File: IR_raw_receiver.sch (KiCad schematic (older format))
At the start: 22 parts, among them IC1 ATtiny85, P1 CONN_6, Q1 8MHz, U1 TSOP38238, U2 L78L05

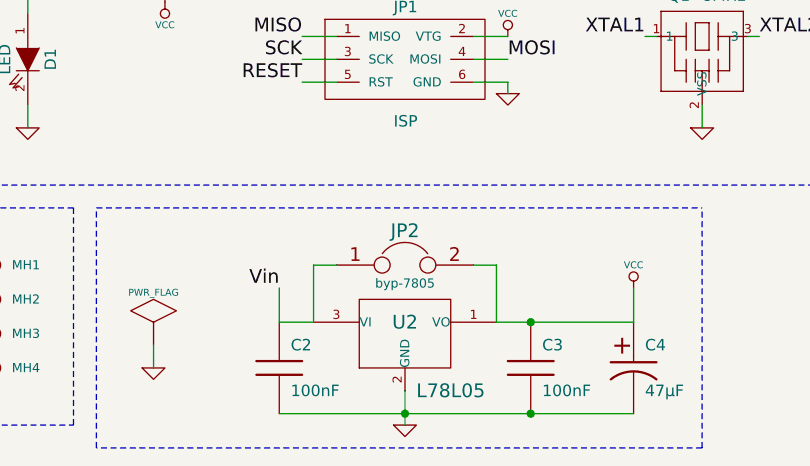
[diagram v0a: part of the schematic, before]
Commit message: V1.20 = shrinked version of V1.10 (standing resistors...)
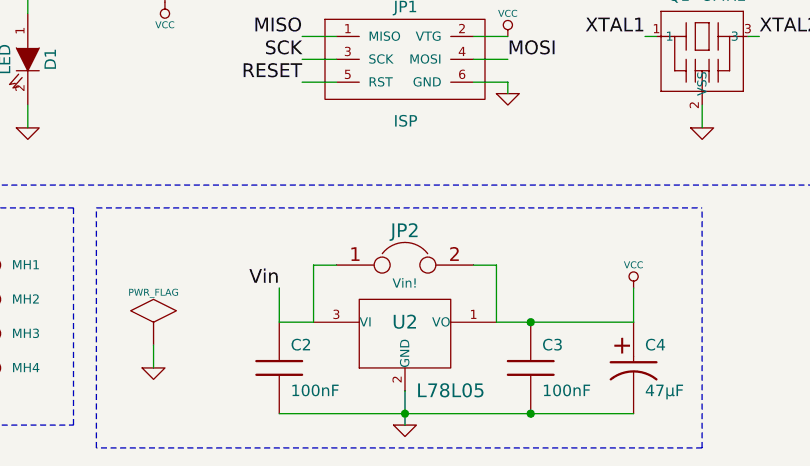
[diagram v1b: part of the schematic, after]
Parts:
- JP2: value byp-7805 -> Vin!
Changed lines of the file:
@@
-EESchema Schematic File Version 2  date Sat 31 Mar 2012 04:20:52 PM CEST
+EESchema Schematic File Version 2  date Sat 31 Mar 2012 08:07:43 PM CEST
 LIBS:power
 LIBS:device
@@
 Title "IR_raw_receiver"
 Date "31 mar 2012"
-Rev "1.10"
+Rev "1.20"
 Comp "2012 - blog.spitzenpfeil.org"
 Comment1 ""
@@
 P 3300 3700
 F 0 "JP2" H 3300 3850 60  0000 C CNN
-F 1 "byp-7805" H 3300 3620 40  0000 C CNN
+F 1 "Vin!" H 3300 3620 40  0000 C CNN
 	1    3300 3700
 	1    0    0    -1
